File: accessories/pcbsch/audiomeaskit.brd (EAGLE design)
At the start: 44.4 x 20.3 mm, 27 parts, among them IC25 INA331IDGK

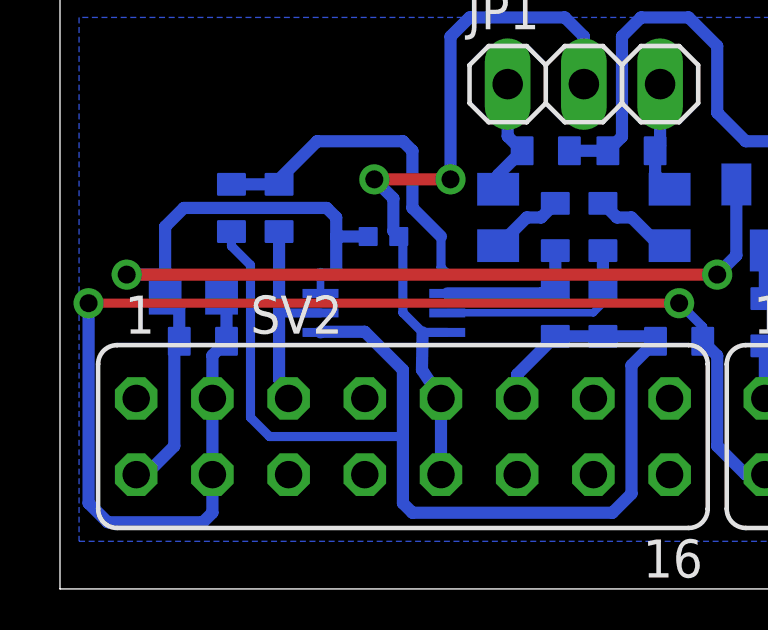
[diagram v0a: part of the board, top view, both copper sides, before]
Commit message: added sync on fpga and fix some things on audiomeaskit
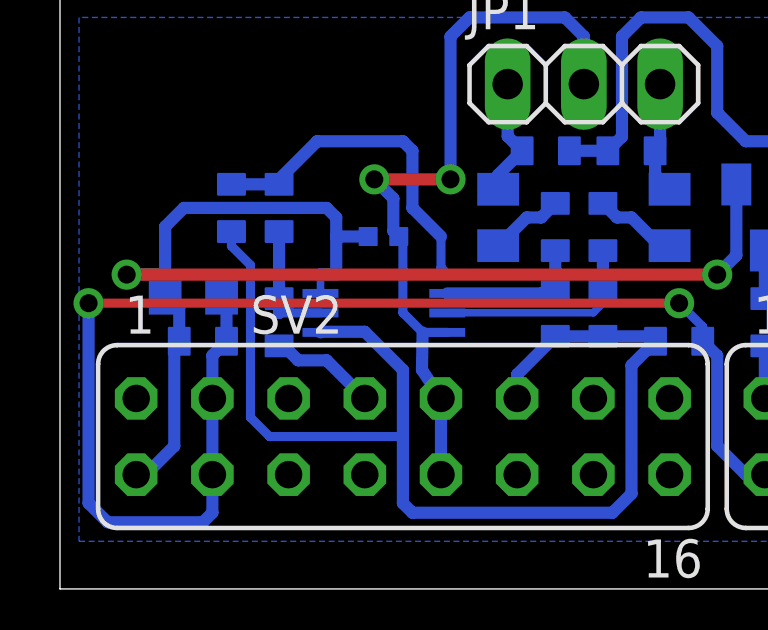
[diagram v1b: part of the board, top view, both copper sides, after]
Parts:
- added C5: 100nF, passive:0603
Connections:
- new net AINRX: C5.1, IC25.6, R202.2
- net AINL: now also SV2.8; no longer SV2.6
- net AINR: now also C5.2, SV2.7; no longer IC25.6, R202.2, SV2.5
- net AOUTL: now also SV2.6; no longer SV2.8
- net AOUTR: now also SV2.5; no longer SV2.7
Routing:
- net AINRX: track 0.00 -> 4.57 mm
- net AINR: track 7.08 -> 3.58 mm
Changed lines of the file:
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@@
 <element name="C4" library="passive" package="0603" value="100nF" x="20.6375" y="8.255" rot="MR0"/>
 <element name="JP1" library="pinhead" package="1X03" value="" x="17.4625" y="16.8275"/>
+<element name="C5" library="passive" package="0603" value="100nF" x="7.3025" y="8.89" rot="MR270"/>
 </elements>
 <signals>
@@
 </signal>
 <signal name="AINR">
-<contactref element="R202" pad="2"/>
-<contactref element="IC25" pad="6"/>
-<contactref element="SV2" pad="5"/>
-<wire x1="7.62" y1="6.35" x2="7.62" y2="6.6675" width="0.4064" layer="16"/>
-<wire x1="7.62" y1="6.6675" x2="7.3025" y2="6.985" width="0.4064" layer="16"/>
-<wire x1="7.3025" y1="11.9126" x2="7.3025" y2="9.2075" width="0.4064" layer="16"/>
-<wire x1="7.3025" y1="9.2075" x2="7.3025" y2="6.985" width="0.4064" layer="16"/>
-<wire x1="8.6831" y1="9.2006" x2="7.3094" y2="9.2006" width="0.3048" layer="16"/>
-<wire x1="7.3094" y1="9.2006" x2="7.3025" y2="9.2075" width="0.3048" layer="16"/>
+<contactref element="SV2" pad="7"/>
+<contactref element="C5" pad="2"/>
+<wire x1="7.3025" y1="8.1026" x2="7.4549" y2="8.1026" width="0.4064" layer="16"/>
+<wire x1="7.4549" y1="8.1026" x2="7.9375" y2="7.62" width="0.4064" layer="16"/>
+<wire x1="7.9375" y1="7.62" x2="8.89" y2="7.62" width="0.4064" layer="16"/>
+<wire x1="8.89" y1="7.62" x2="10.16" y2="6.35" width="0.4064" layer="16"/>
 </signal>
 <signal name="N$225">
@@
 <wire x1="19.8374" y1="13.8049" x2="20.32" y2="13.3223" width="0.4064" layer="16"/>
 </signal>
-<signal name="AOUTL">
+<signal name="AOUTR">
+<contactref element="SV2" pad="5"/>
+</signal>
+<signal name="AINL">
 <contactref element="SV2" pad="8"/>
-</signal>
-<signal name="AOUTR">
-<contactref element="SV2" pad="7"/>
-</signal>
-<signal name="AINL">
-<contactref element="SV2" pad="6"/>
 </signal>
 <signal name="S1">
@@
 <contactref element="SV1" pad="15"/>
 </signal>
+<signal name="AOUTL">
+<contactref element="SV2" pad="6"/>
+</signal>
+<signal name="AINRX">
+<contactref element="R202" pad="2"/>
+<contactref element="IC25" pad="6"/>
+<wire x1="7.3025" y1="11.9126" x2="7.3025" y2="9.6774" width="0.4064" layer="16"/>
+<wire x1="7.3025" y1="9.6774" x2="7.3025" y2="9.2075" width="0.4064" layer="16"/>
+<wire x1="8.6831" y1="9.2006" x2="7.3094" y2="9.2006" width="0.3048" layer="16"/>
+<wire x1="7.3094" y1="9.2006" x2="7.3025" y2="9.2075" width="0.3048" layer="16"/>
+<contactref element="C5" pad="1"/>
+<wire x1="7.3094" y1="9.2006" x2="7.3094" y2="9.6705" width="0.4064" layer="16"/>
+<wire x1="7.3094" y1="9.6705" x2="7.3025" y2="9.6774" width="0.4064" layer="16"/>
+</signal>
 </signals>
